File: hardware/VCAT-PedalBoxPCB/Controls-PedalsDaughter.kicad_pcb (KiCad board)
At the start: 2 copper layers, 53 x 58.6 mm, 53 parts, among them J1 MX150_02x03_Vertical, J6 MX150_02x10_Vertical, U1 TLV9301xDCK, U2 LDO40LPURY, U3 TLV9301xDCK, U4 INA241A5xD, U6 LDO40LPURY

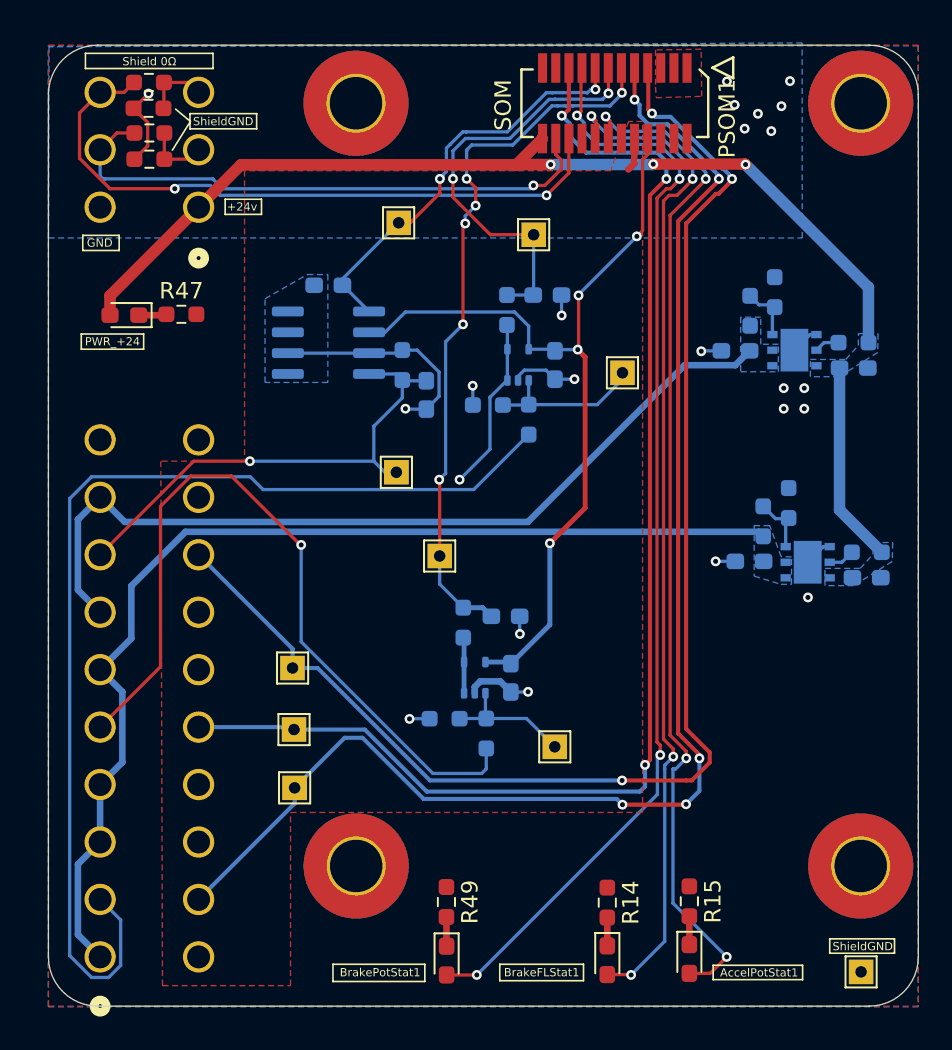
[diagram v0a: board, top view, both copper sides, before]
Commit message: updated mx150 pin order :( works now
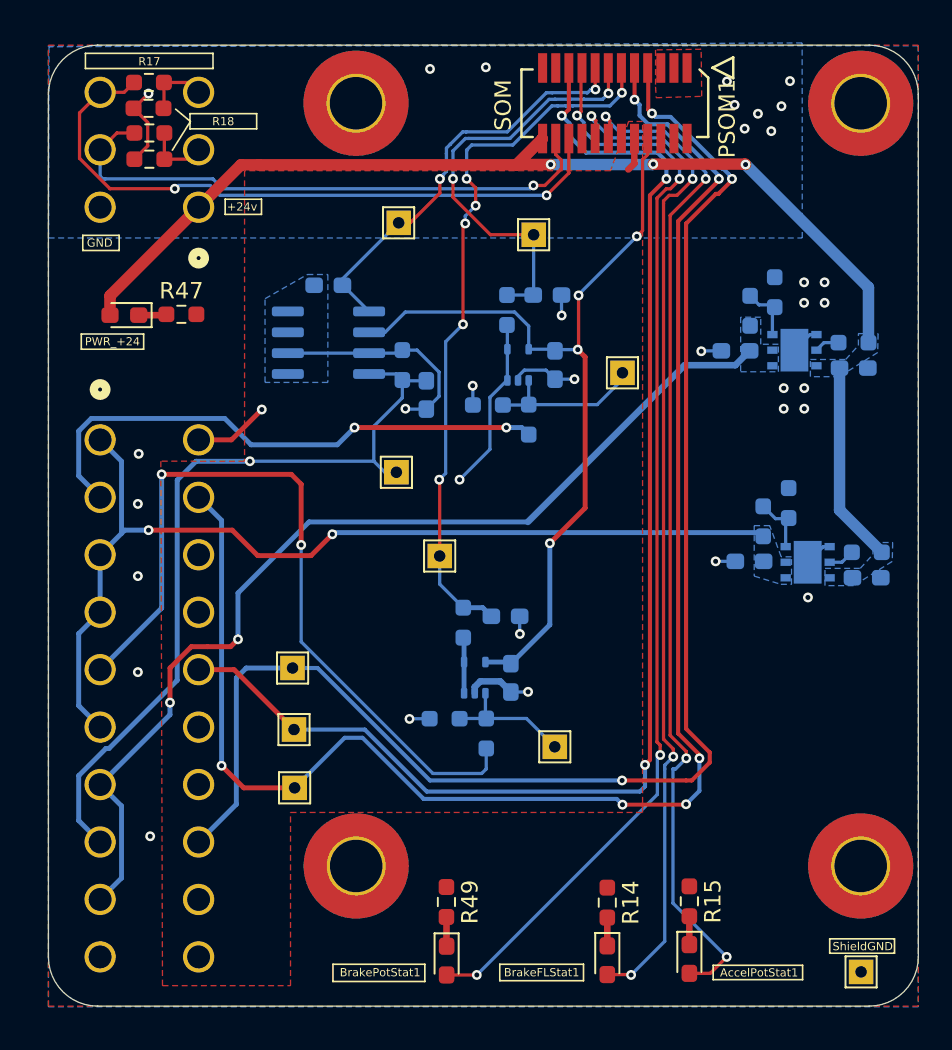
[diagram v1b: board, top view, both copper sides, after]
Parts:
- J6: footprint UTSVT_Connectors:CONN_SD-75757-002_2X10_F16p09_MOL -> UTSVT_Connectors:MX150_02x10_Vertical
- R17: renamed from Shield 0Ω
- renumbered ShieldGND to R18
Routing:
- net /BrakePot_Main: track 66.6 -> 33.9 mm, vias 0 -> 2
- net /BrakeFL_Main: track 30.0 -> 48.6 mm
- net /BrakePotRedundant: track 85.6 -> 98.3 mm, vias 5 -> 6
- net +9V: track 52.6 -> 61.9 mm, vias 0 -> 2
- net +5V: track 65.6 -> 60.2 mm, vias 0 -> 2
- net /BrakeFLRedundant: track 84.9 -> 90.3 mm
- net GNDA: track 28.6 -> 33.2 mm, vias 7 -> 8
- net /AccelPotRedundant: track 78.7 -> 80.3 mm
- net /Accel_Main: track 47.9 -> 47.8 mm, vias 1 -> 2
- net GND: vias 15 -> 26

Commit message: Final review..(?)
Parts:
- added R16: 0.075, Resistor_SMD:R_0603_1608Metric_Pad0.98x0.95mm_HandSolder, B.Cu at (159.3, 91.6)
- R1: value 0.175 -> 0.1
- Shield GND: renamed from R17
- Shielding 0Ω: renamed from R18
- moved C5 39.8 mm to (136.8, 82.5), turned to 180 degrees
- moved R10 38.3 mm to (136.8, 84.0)
- moved U2 34.2 mm to (136.4, 87.5), turned to -90 degrees
- moved R7 34.1 mm to (133.8, 87.4)
- moved R6 29.7 mm to (136.4, 90.2), turned to 180 degrees
- moved Brake_GPIO1 29.6 mm to (171.0, 103.7)
- moved C4 29.2 mm to (136.4, 91.7)
- moved C7 28.4 mm to (142.6, 83.2), turned to 180 degrees
- moved Brake_Fl_Sn1 28.3 mm to (163.9, 99.8)
- moved R13 27.7 mm to (142.6, 84.7)
- moved R9 25.4 mm to (139.8, 87.5)
- moved U6 24.0 mm to (142.5, 87.4), turned to -90 degrees
- moved R4 23.8 mm to (153.5, 89.6)
- moved C3 23.1 mm to (155.8, 87.2)
- moved U3 23.1 mm to (153.6, 87.2)
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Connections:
- PSOM1 pad 12: unconnected-(PSOM1-SPI2_NSS-Pad12) -> /BrakePotStatus
- PSOM1 pad 13: /BrakePot_GPIO -> /BrakeFLRedundant
- PSOM1 pad 14: /AccelPotStatus -> unconnected-(PSOM1-SPI2_MISO-Pad14)
- PSOM1 pad 15: /BrakeFL_GPIO -> /AccelPotRedundant
- PSOM1 pad 16: /BrakeFluidStatus -> unconnected-(PSOM1-SPI2_MOSI-Pad16)
- PSOM1 pad 17: /BrakePotStatus -> unconnected-(PSOM1-SPI1_MOSI-Pad17)
- PSOM1 pad 19: /AccelPotRedundant -> /BrakePotRedundant
- PSOM1 pad 4: unconnected-(PSOM1-I2C1_SDA-Pad4) -> /AccelPotStatus
- PSOM1 pad 6: unconnected-(PSOM1-I2C1_SCL-Pad6) -> /BrakeFluidStatus
- PSOM1 pad 7: /BrakeFLRedundant -> /BrakePot_GPIO
- PSOM1 pad 9: /BrakePotRedundant -> /BrakeFL_GPIO
- R1 pad 2: GNDA -> Net-(R1-Pad2)
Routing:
- net +24V: track 71.7 -> 31.5 mm, vias 3 -> 0
- net /BrakePotRedundant: track 98.3 -> 64.3 mm, vias 6 -> 3
- net GND: track 12.0 -> 45.2 mm, vias 26 -> 53
- net +VDDA: track 52.5 -> 24.8 mm
- net +5V: track 60.2 -> 34.2 mm, vias 2 -> 0
- net Net-(U3-+): track 8.08 -> 31.4 mm, vias 0 -> 2
- net /BrakePot_Main: track 33.9 -> 56.4 mm, vias 2 -> 4
- net /BrakeFLRedundant: track 90.3 -> 68.1 mm
- net /AccelPotRedundant: track 80.3 -> 60.4 mm
- net /BrakePot_GPIO: track 26.5 -> 45.7 mm, vias 2 -> 3
- net /BrakeFL_Main: track 48.6 -> 65.9 mm
- net Net-(U1-+): track 9.81 -> 26.2 mm
- net +9V: track 61.9 -> 45.7 mm, vias 2 -> 1
- net /Accel_GPIO: track 44.1 -> 56.5 mm, vias 6 -> 5
- net GNDA: track 33.2 -> 44.6 mm, vias 8 -> 15
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- removed copper zone on F.Cu, net GNDA
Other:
- board text added: "+24v GND"
- board text added: "5V GNDA"
- board text added: "9V 5V Adj LDO"
- board text added: "9V GNDA"
- board text added: "AccelPot AccelPot Red"
- board text added: "BrFL BrFL Red"
- board text added: "BrPot BrPot Red"
- board text added: "CANH Out CANH In"
- board text added: "CANL Out CANL In"
- board text added: "SOM"
- board text removed: "Adj LDO 5V"
- board text removed: "Adj LDO 9V"

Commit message: bruh
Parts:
- removed Brake_GPIO1: Accel, TestPoint:TestPoint_THTPad_1.5x1.5mm_Drill0.7mm
- removed C1: 0.01uf, Capacitor_SMD:C_0603_1608Metric_Pad1.08x0.95mm_HandSolder
- removed C3: 0.1uf, Capacitor_SMD:C_0603_1608Metric_Pad1.08x0.95mm_HandSolder
- removed R11: 100, Resistor_SMD:R_0603_1608Metric_Pad0.98x0.95mm_HandSolder
- removed R2: 10k, Resistor_SMD:R_0603_1608Metric_Pad0.98x0.95mm_HandSolder
- removed R4: 22k, Resistor_SMD:R_0603_1608Metric_Pad0.98x0.95mm_HandSolder
- removed Shield GND: 0, Resistor_SMD:R_0603_1608Metric_Pad0.98x0.95mm_HandSolder
- removed U1, U3: TLV9301xDCK, Package_TO_SOT_SMD:SOT-353_SC-70-5
- added BrakePot GPIO: Accel, TestPoint:TestPoint_THTPad_1.5x1.5mm_Drill0.7mm, F.Cu at (169.9, 111.1)
- added C11: 0.1uF, Capacitor_SMD:C_0603_1608Metric_Pad1.08x0.95mm_HandSolder, B.Cu at (170.9, 85.3)
- added R18: 0, Resistor_SMD:R_0603_1608Metric_Pad0.98x0.95mm_HandSolder, F.Cu at (127.2, 74.5)
- added R21: 22k, Resistor_SMD:R_0603_1608Metric_Pad0.98x0.95mm_HandSolder, B.Cu at (168.1, 96.2)
- added R22: 100, Resistor_SMD:R_0603_1608Metric_Pad0.98x0.95mm_HandSolder, B.Cu at (167.7, 85.2)
- added R23: 100, Resistor_SMD:R_0603_1608Metric_Pad0.98x0.95mm_HandSolder, B.Cu at (166.1, 85.2)
- added U5: TLV9002QDRQ1, TLV9002QDRQ1:SOIC8_D_TEX, B.Cu at (168.3, 90.7)
- C2: value 0.1uf -> 0.01uf
- PWR +24: renamed from PWR_+24
- R12: value 100 -> 10k
- moved R3 12.9 mm to (169.6, 96.2), turned to -90 degrees
- moved R12 9.64 mm to (166.5, 96.2), turned to -90 degrees
- moved BrakeRaw1 7.32 mm to (170.0, 107.1)
- moved Brake_Fl_Sn1 7.32 mm to (162.7, 107.0)
- moved Brake_Fl_Sn_Raw1 7.32 mm to (162.7, 111.2)
- moved Accel_GPIO1 7.32 mm to (162.8, 115.4)
- moved AccelRaw1 7.32 mm to (169.9, 115.0)
- moved R5 6.73 mm to (171.9, 90.7), turned to 90 degrees
- moved C6 5.89 mm to (164.6, 85.3), turned to 90 degrees
- moved C2 3.88 mm to (169.3, 85.2), turned to 90 degrees
- moved C10 3.87 mm to (158.8, 92.0)
- moved C9 3.87 mm to (157.0, 84.0)
- moved R1 3.87 mm to (157.2, 92.0)
- moved R16 3.87 mm to (155.5, 92.0)
- moved U4 3.87 mm to (157.1, 87.5)
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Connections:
- AccelRaw1 pad 1: Net-(U3-+) -> Net-(U5-IN1+)
- Accel_GPIO1 pad 1: /Accel_GPIO -> /BrakePot_GPIO
- BrakeRaw1 pad 1: Net-(U1-+) -> Net-(U5-IN2+)
- C2 pad 2: +VDDA -> /BrakePot_GPIO
- C6 pad 2: /BrakePot_GPIO -> /Accel_GPIO
- R12 pad 1: /BrakePot_GPIO -> Net-(U5-IN2+)
- R12 pad 2: Net-(U1--) -> /BrakePot_Main
- R3 pad 1: Net-(U1-+) -> Net-(U5-IN1+)
- R3 pad 2: /BrakePot_Main -> /Accel_Main
- R5 pad 1: Net-(U1-+) -> Net-(U5-IN1+)
- Shielding 0Ω pad 1: GND -> /CANL
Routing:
- net Net-(U3-+): track 31.4 -> 0.00 mm, vias 2 -> 0
- net Net-(U5-IN1+): track 0.00 -> 29.3 mm
- net Net-(U1-+): track 26.2 -> 0.00 mm
- net /Accel_Main: track 40.1 -> 59.6 mm, vias 1 -> 5
- net Net-(U5-IN2+): track 0.00 -> 17.5 mm
- net /BrakePot_GPIO: track 45.7 -> 59.1 mm, vias 3 -> 5
- net +VDDA: track 24.8 -> 11.7 mm, vias 4 -> 3
- net /BrakePot_Main: track 56.4 -> 44.2 mm, vias 4 -> 2
- net /BrakeFL_GPIO: track 36.5 -> 46.5 mm, vias 3 -> 5
- net Net-(U5-IN1-): track 0.00 -> 9.77 mm, vias 0 -> 2
- net GNDA: track 44.6 -> 54.2 mm, vias 15 -> 17
- net GND: track 45.2 -> 37.4 mm, vias 53 -> 50
- net Net-(U5-IN2-): track 0.00 -> 7.25 mm
- net /Accel_GPIO: track 56.5 -> 50.1 mm, vias 5 -> 3
- net /BrakeFL_Main: track 65.9 -> 71.7 mm, vias 1 -> 3
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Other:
- board text added: "5V"
- board text added: "9V"
- board text added: "AccelPot Red"
- board text added: "Accel_Pot"
- board text added: "BrFL Red"
- board text added: "BrPot Red"
- board text added: "BrakeFL"
- board text added: "BrakePot"
- board text added: "GNDA"
- board text added: "NC"
- board text removed: "5V GNDA"
- board text removed: "9V GNDA"
- board text removed: "AccelPot AccelPot Red"
- board text removed: "BrFL BrFL Red"
- board text removed: "BrPot BrPot Red"

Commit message: bruh2
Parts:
- removed BrakePot GPIO: Accel, TestPoint:TestPoint_THTPad_1.5x1.5mm_Drill0.7mm
- removed PWR +24: PedalsBoard_Status_Red, LED_SMD:LED_0603_1608Metric_Pad1.05x0.95mm_HandSolder
- added 9V: 9V_Out, TestPoint:TestPoint_Pad_1.0x1.0mm, F.Cu at (136.6, 101.8)
- added Adj5v: Adj5V, TestPoint:TestPoint_Pad_1.0x1.0mm, F.Cu at (130.2, 91.5)
- added Adj9V: Adj9V, TestPoint:TestPoint_Pad_1.0x1.0mm, F.Cu at (139.2, 90.9)
- added BrakePot_GPIO1: Accel, TestPoint:TestPoint_THTPad_1.5x1.5mm_Drill0.7mm, F.Cu at (169.8, 111.3)
- added En5v: Enable5V, TestPoint:TestPoint_Pad_1.0x1.0mm, F.Cu at (131.8, 88.9)
- added En9V: Enable9V, TestPoint:TestPoint_Pad_1.0x1.0mm, F.Cu at (145.8, 88.9)
- added GND: GND, TestPoint:TestPoint_Pad_1.0x1.0mm, F.Cu at (164.7, 74.7)
- added PWR_+24: PedalsBoard_Status_Red, LED_SMD:LED_0603_1608Metric_Pad1.05x0.95mm_HandSolder, F.Cu at (125.7, 87.2)
- added TP6: 5V_Out, TestPoint:TestPoint_Pad_1.0x1.0mm, F.Cu at (127.4, 91.5)
- added Vin: Vin, TestPoint:TestPoint_Pad_1.0x1.0mm, F.Cu at (139.9, 81.0)
- moved Shielding 0Ω 0.13 mm to (127.1, 73.0)
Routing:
- net Net-(U2-EN): track 2.31 -> 10.9 mm, vias 0 -> 1
- net Net-(U6-EN): track 1.70 -> 8.26 mm, vias 0 -> 1
- net Net-(U2-ADJ): track 3.20 -> 9.08 mm, vias 0 -> 1
- net +9V: track 45.7 -> 51.1 mm
- net Net-(U6-ADJ): track 3.26 -> 6.13 mm, vias 0 -> 1
- net +5V: track 34.2 -> 36.8 mm, vias 0 -> 1
- net /CANL: track 35.9 -> 37.0 mm
- net +24V: vias 0 -> 1

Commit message: LeGoat
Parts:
- added G***: LOGO, Graphics:LeGoat, F.Cu at (155.1, 97.5)
- added G***: LOGO, UTSVT_Logos:roosters, F.Cu at (152.0, 101.3)
- added G***: LOGO, UTSVT_Logos:UTSVT_Logo_Symbol, F.Cu at (153.0, 76.5)
- added G***: LHRs_LOGO, UTSVT_Logos:LHRs_LOGO, F.Cu at (133.1, 89.6)
- added G***: LOGO, UTSVT_Logos:Hallock_Image_Tiny, F.Cu at (155.0, 121.2)
- 9V, Adj5v, Adj9V, En5v, En9V, TP6, Vin: moved to B.Cu
- moved Raw6 36.1 mm to (134.3, 126.6)
- moved AccelPotStat1 10.2 mm to (149.9, 125.1)
- moved R15 10.2 mm to (149.9, 121.6)
- moved R14 7.49 mm to (147.7, 121.6)
- moved BrakeFLStat1 7.49 mm to (147.7, 125.1)
- moved BrakePotStat1 1.35 mm to (145.3, 125.2)
- moved R49 1.35 mm to (145.3, 121.6)
- moved Adj9V 0.61 mm to (139.7, 90.5), turned to 180 degrees
- turned 9V to 180 degrees
- turned Adj5v to 180 degrees
- turned En5v to 180 degrees
- turned En9V to 180 degrees
- turned TP6 to 180 degrees
- turned Vin to 180 degrees
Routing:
- net /AccelPotStatus: track 71.4 -> 63.3 mm, vias 4 -> 2
- net /BrakeFluidStatus: track 66.7 -> 62.8 mm
- net /BrakePotStatus: track 59.6 -> 58.1 mm
- net Net-(U6-ADJ): track 6.13 -> 5.49 mm, vias 1 -> 0
- net +9V: vias 1 -> 2
- net Net-(U6-EN): track 8.26 -> 8.27 mm, vias 1 -> 2
- net Net-(U2-EN): vias 1 -> 0
- net Net-(U2-ADJ): vias 1 -> 0
- net +5V: vias 1 -> 0
- net +24V: vias 1 -> 0
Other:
- board text added: "Pedals Board Nov 12th, 2025 Sathvik Yechuri, RevA"
